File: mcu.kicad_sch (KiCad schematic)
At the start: 17 parts, among them J2 Conn_ARM_SWD_TagConnect_TC2030, U3 STM32L053R8Tx

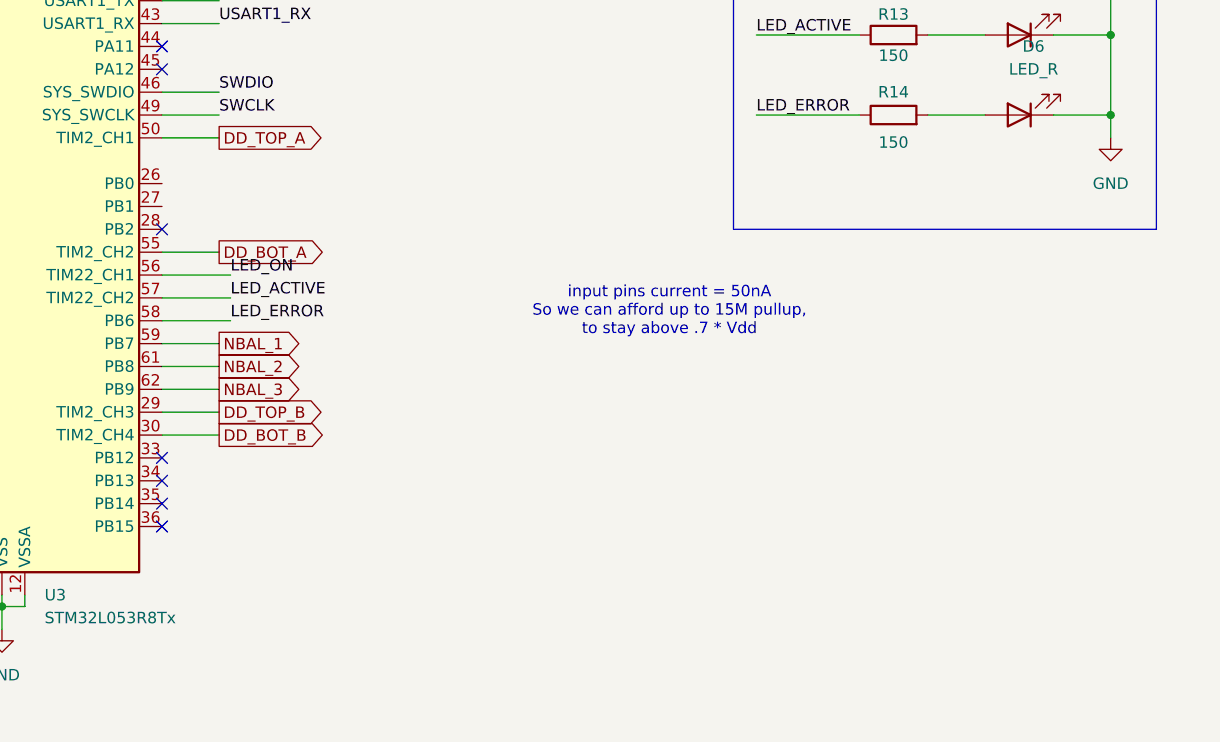
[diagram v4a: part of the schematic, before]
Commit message: Adding switch, moving current sense
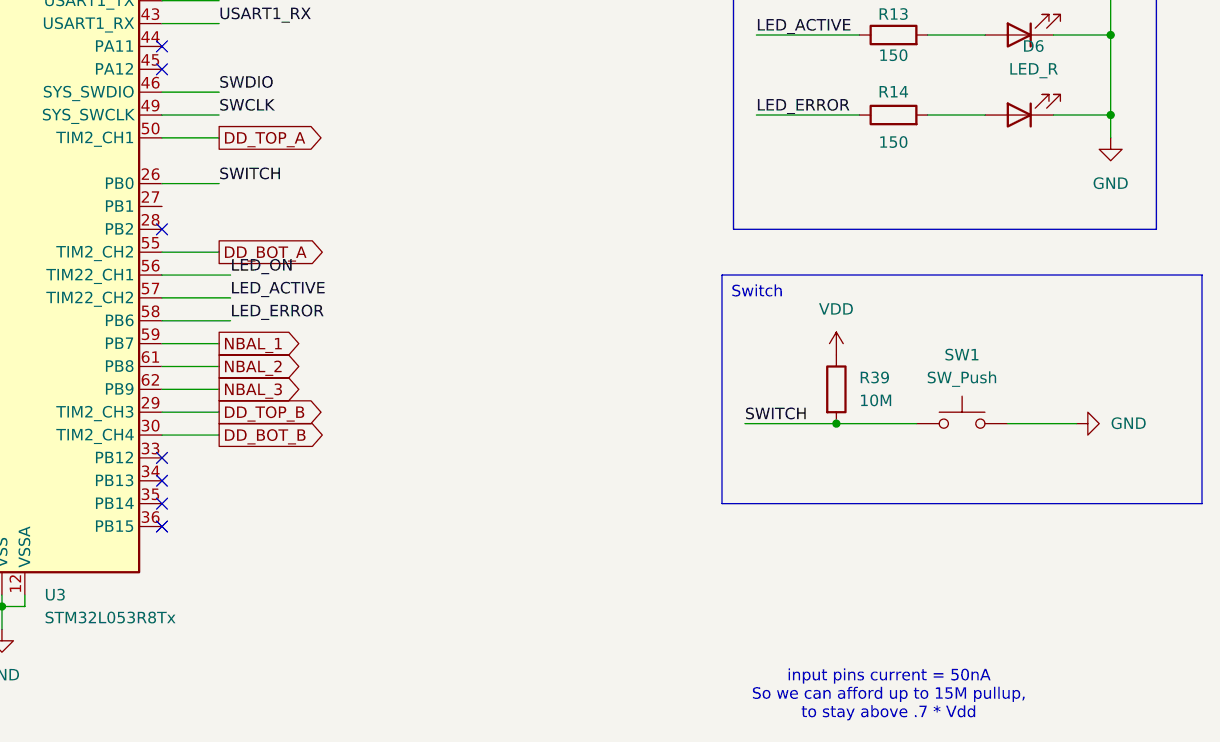
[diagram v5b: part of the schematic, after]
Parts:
- added R39: 10M, symbol Device:R
- added SW1: SW_Push, Button_Switch_SMD:SW_Push_1P1T_XKB_TS-1187A, symbol Switch:SW_Push
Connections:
- net GND: now also SW1.2
- net VDD: now also R39.1
- net SWITCH: now reaches U3.26 (PB0)
- net SWITCH: now also R39.2, SW1.1

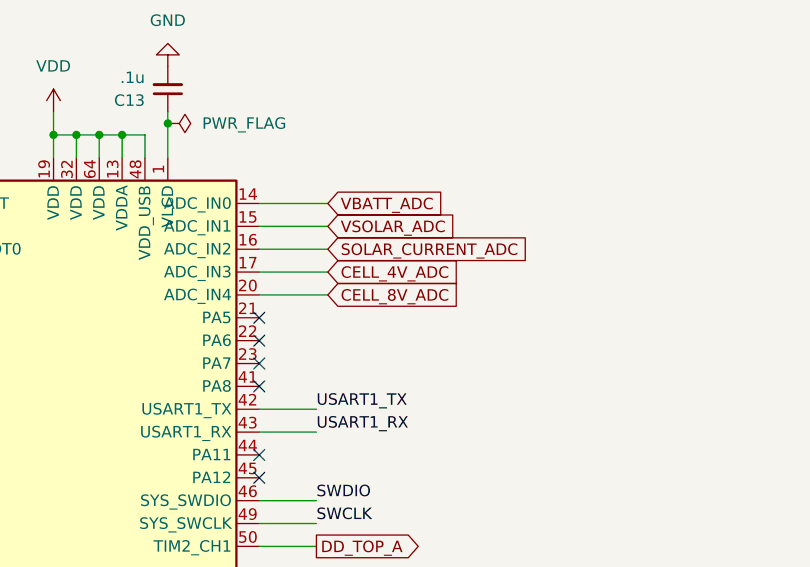
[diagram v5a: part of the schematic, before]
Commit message: Starting draft of ADC multiplexer
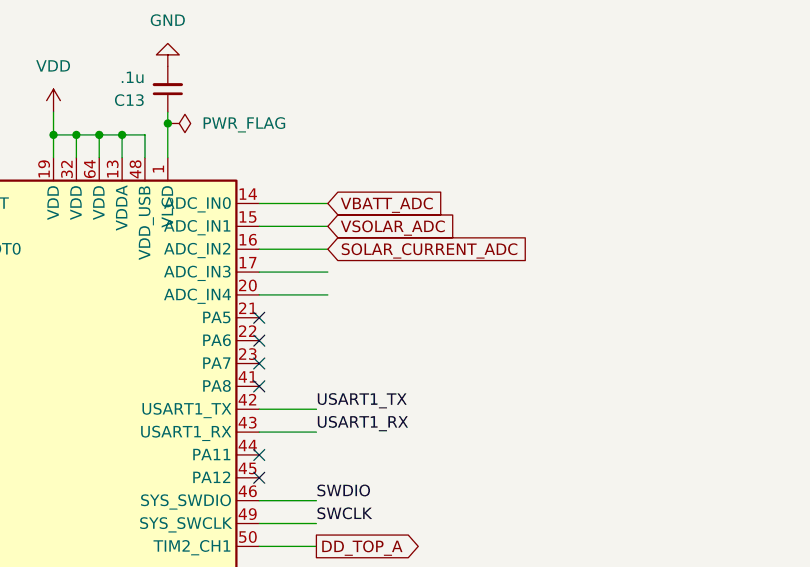
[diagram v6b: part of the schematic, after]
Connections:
- net CELL_4V_ADC: no longer names the net of U3.17 (PA3)
- net CELL_8V_ADC: no longer names the net of U3.20 (PA4)
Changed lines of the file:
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@@
-		)
-	)
-	(global_label "CELL_8V_ADC"
-		(shape input)
-		(at 166.37 60.96 0)
-		(fields_autoplaced yes)
-		(effects
-			(font
-				(size 1.27 1.27)
-			)
-			(justify left)
-		)
-		(property "Intersheetrefs" "${INTERSHEET_REFS}"
-			(at 181.6923 60.96 0)
-			(effects
-				(font
-					(size 1.27 1.27)
-				)
-				(justify left)
-				(hide yes)
-			)
 		)
 	)
@@
 			(effects
 				(font
-					(size 1.27 1.27)
-				)
-				(justify left)
-				(hide yes)
-			)
-		)
-	)
-	(global_label "CELL_4V_ADC"
-		(shape input)
-		(at 166.37 58.42 0)
-		(fields_autoplaced yes)
-		(effects
-			(font
-				(size 1.27 1.27)
-			)
-			(justify left)
-		)
-		(property "Intersheetrefs" "${INTERSHEET_REFS}"
-			(at 181.6923 58.42 0)
-			(effects
-				(font

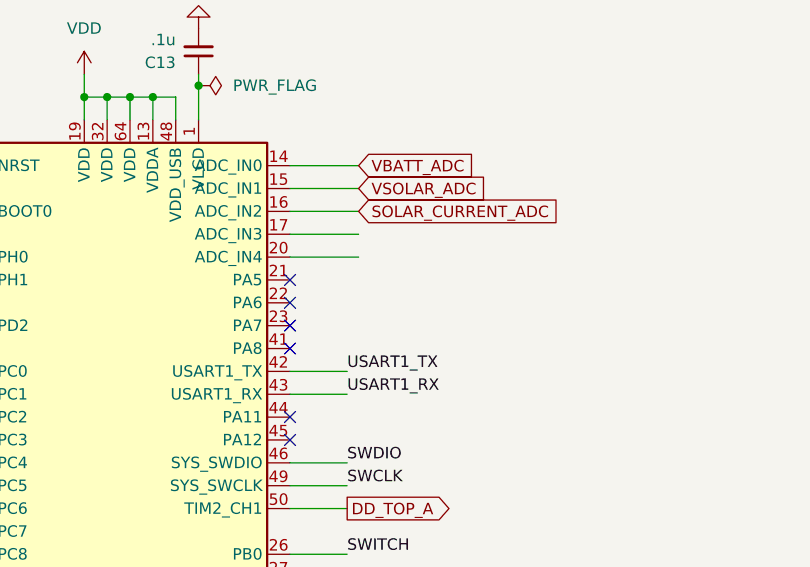
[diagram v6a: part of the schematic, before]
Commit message: Adding ADC multiplexer, protection diodes
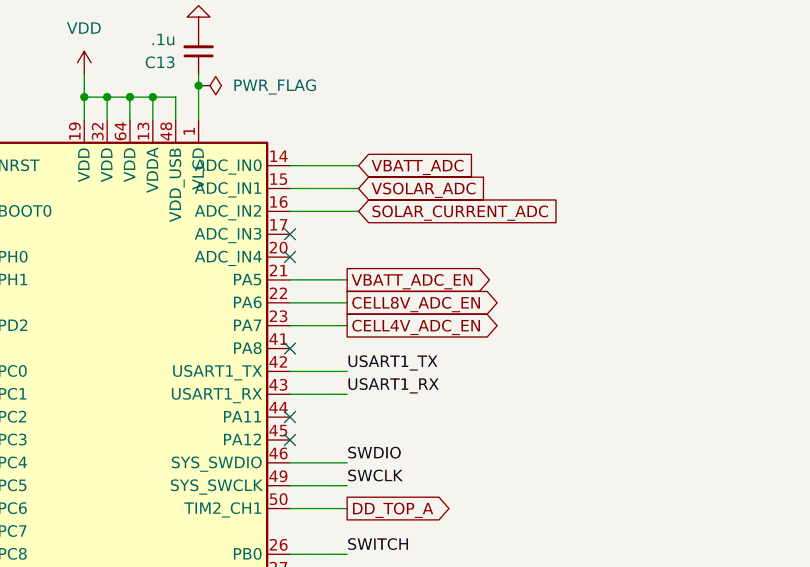
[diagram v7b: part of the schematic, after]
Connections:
- net VBATT_ADC_EN: now reaches U3.21 (PA5)
- net CELL8V_ADC_EN: now reaches U3.22 (PA6)
- net CELL4V_ADC_EN: now reaches U3.23 (PA7)
- no-connect marks 31 -> 30
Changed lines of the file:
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@@
 	)
 	(no_connect
-		(at 158.75 63.5)
+		(at 158.75 60.96)
 	)
 	(no_connect
@@
 	)
 	(no_connect
+		(at 158.75 58.42)
+	)
+	(no_connect
 		(at 68.58 41.91)
 	)
@@
 	)
 	(no_connect
-		(at 158.75 68.58)
-	)
-	(no_connect
 		(at 123.19 73.66)
 	)
@@
 	)
 	(no_connect
-		(at 158.75 66.04)
-	)
-	(no_connect
 		(at 123.19 60.96)
 	)
@@
 	(wire
 		(pts
+			(xy 158.75 66.04) (xy 165.1 66.04)
+		)
+		(stroke
+			(width 0)
+			(type default)
+		)
+	)
+	(wire
+		(pts
 			(xy 224.79 86.36) (xy 236.22 86.36)
 		)
@@
 	(wire
 		(pts
+			(xy 165.1 63.5) (xy 158.75 63.5)
+		)
+		(stroke
+			(width 0)
+			(type default)
+		)
+	)
+	(wire
+		(pts
 			(xy 165.1 101.6) (xy 158.75 101.6)
 		)
@@
 	(wire
 		(pts
-			(xy 166.37 58.42) (xy 158.75 58.42)
-		)
-		(stroke
-			(width 0)
-			(type default)
-		)
-	)
-	(wire
-		(pts
 			(xy 68.58 36.83) (xy 73.66 36.83)
 		)
@@
 	(wire
 		(pts
-			(xy 166.37 60.96) (xy 158.75 60.96)
-		)
-		(stroke
-			(width 0)
-			(type default)
-		)
-	)
-	(wire
-		(pts
 			(xy 242.57 33.02) (xy 242.57 34.29)
 		)
@@
 		(pts
 			(xy 140.97 43.18) (xy 138.43 43.18)
+		)
+		(stroke
+			(width 0)
+			(type default)
+		)
+	)
+	(wire
+		(pts
+			(xy 158.75 68.58) (xy 165.1 68.58)
 		)
 		(stroke
@@
 				(hide yes)
 			)
+		)
+	)
+	(global_label "CELL4V_ADC_EN"
+		(shape output)
+		(at 165.1 68.58 0)
+		(effects
+			(font
+				(size 1.27 1.27)
+			)
+			(justify left)
+		)
+		(property "Intersheetrefs" "${INTERSHEET_REFS}"
+			(at 165.1 68.58 0)
+			(effects
+				(font
+					(size 1.27 1.27)
+				)
+				(hide yes)
+			)
+		)
+	)
+	(global_label "VBATT_ADC_EN"
+		(shape output)
+		(at 165.1 63.5 0)
+		(effects
+			(font
+				(size 1.27 1.27)
+			)
+			(justify left)
+		)
+		(property "Intersheetrefs" "${INTERSHEET_REFS}"
+			(at 165.1 63.5 0)
+			(effects
+				(font
+					(size 1.27 1.27)
+				)
+				(hide yes)
+			)
+		)
+	)
+	(global_label "CELL8V_ADC_EN"
+		(shape output)
+		(at 165.1 66.04 0)
+		(effects
+			(font
+				(size 1.27 1.27)
+			)
+			(justify left)
+		)
+		(property "Intersheetrefs" "${INTERSHEET_REFS}"
+			(at 165.1 66.04 0)
+			(effects
+				(font
+					(size 1.27 1.27)
+				)
+				(hide yes)
+			)

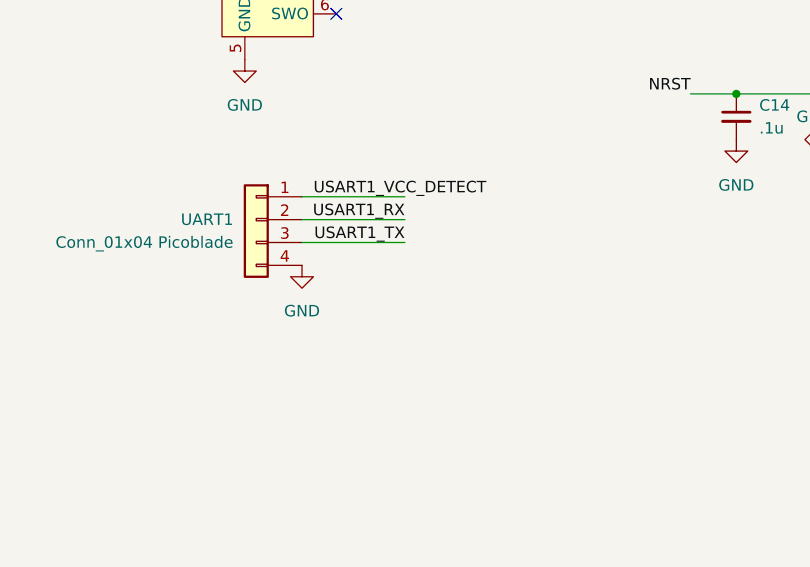
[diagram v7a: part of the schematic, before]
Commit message: Adding new ST driver, protecting uart input
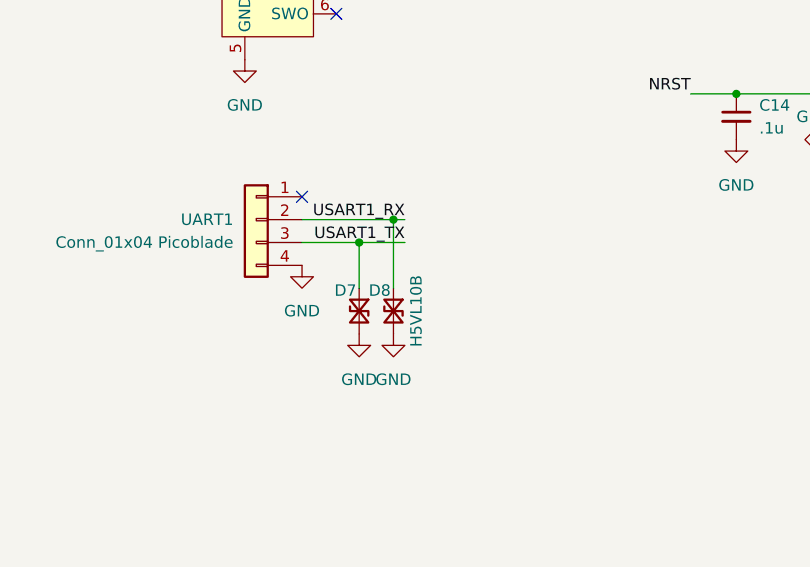
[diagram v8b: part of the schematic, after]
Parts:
- added D7, D8: H5VL10B, Diode_SMD:D_SOD-882, symbol Device:D_TVS_Small
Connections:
- net GND: now also D7.2 (A2), D8.2 (A2)
- net USART1_RX: now also D8.1 (A1)
- net USART1_TX: now also D7.1 (A1)
- net USART1_VCC_DETECT: no longer names the net of UART1.1 (Pin_1)
- no-connect marks 30 -> 31
